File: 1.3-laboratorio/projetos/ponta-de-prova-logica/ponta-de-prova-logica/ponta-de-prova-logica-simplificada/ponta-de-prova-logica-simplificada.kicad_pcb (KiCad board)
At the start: 2 copper layers, 18 parts, among them J1 TEST PROBE, J2 Conn_01x02, U1 LM319

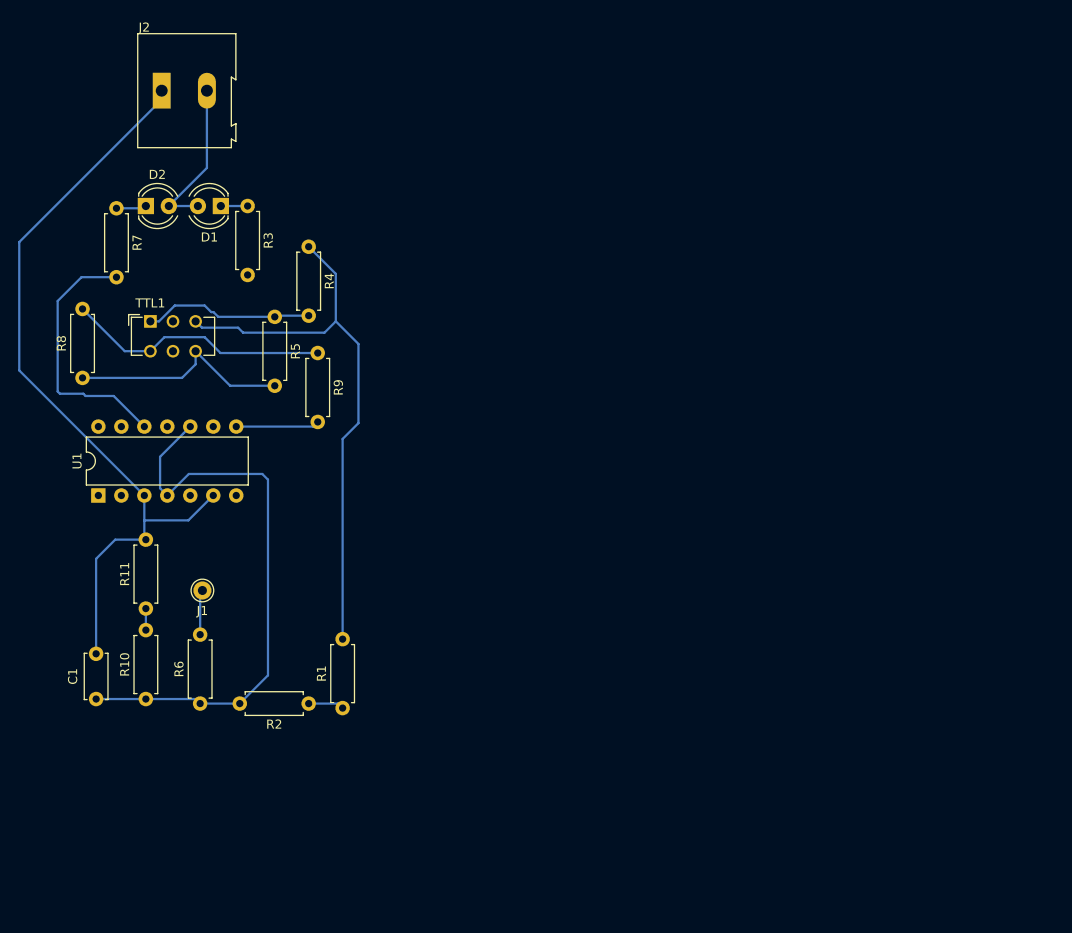
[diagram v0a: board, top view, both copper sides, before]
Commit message: Esquema PCB
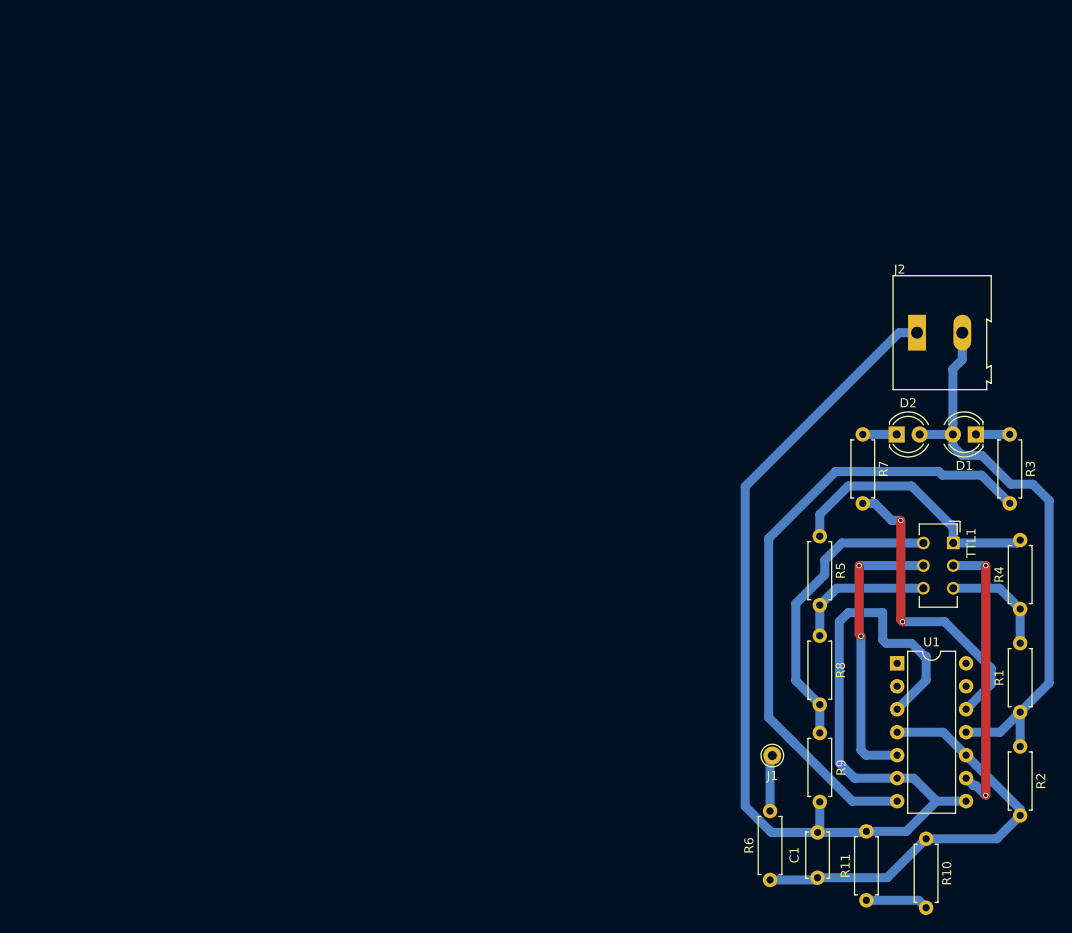
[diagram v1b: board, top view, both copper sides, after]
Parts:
- moved TTL1 92.1 mm to (195.0, 83.5), turned to 270 degrees
- moved U1 90.2 mm to (188.8, 96.8), turned to 0 degrees
- moved R4 88.3 mm to (202.4, 90.8), turned to 90 degrees
- moved R3 88.0 mm to (201.2, 71.5)
- moved J2 87.7 mm to (191.0, 60.2)
- moved R10 87.6 mm to (192.0, 116.2), turned to 270 degrees
- moved D1 87.2 mm to (197.5, 71.5)
- moved D2 86.8 mm to (188.8, 71.5)
- moved R8 86.3 mm to (180.2, 93.8), turned to 270 degrees
- moved R7 86.2 mm to (185.0, 71.5)
- moved R11 85.9 mm to (185.4, 123.0)
- moved C1 82.2 mm to (180.0, 120.5)
- moved R2 78.8 mm to (202.4, 106.0), turned to 270 degrees
- moved R1 74.9 mm to (202.4, 102.2)
- moved R9 69.6 mm to (180.2, 104.5)
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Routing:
- net Net-(R3-Pad2): track 0.00 -> 69.8 mm
- net Net-(R1-Pad2): track 62.9 -> 12.1 mm
- net GND: track 96.8 -> 141.0 mm
- net +5V: track 21.7 -> 65.2 mm
- net Net-(TTL1-Pad2): track 0.00 -> 32.0 mm, vias 0 -> 2
- net Net-(TTL1-Pad5): track 0.00 -> 31.8 mm, vias 0 -> 2
- net Net-(C1-Pad1): track 63.8 -> 48.4 mm
- net Net-(R4-Pad2): track 18.8 -> 29.6 mm
- net Net-(R5-Pad2): track 24.9 -> 15.6 mm
- net Net-(R7-Pad2): track 28.8 -> 33.9 mm, vias 0 -> 2
- net Net-(R10-Pad2): track 2.38 -> 6.94 mm
- net Net-(R8-Pad2): track 29.3 -> 33.2 mm
- net Net-(J1-Pad1): track 4.98 -> 6.23 mm
- net Net-(D1-Pad1): track 2.96 -> 3.75 mm
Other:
- net class Default: trace_width 0.25 -> 1; via_dia 0.8 -> 0.6
